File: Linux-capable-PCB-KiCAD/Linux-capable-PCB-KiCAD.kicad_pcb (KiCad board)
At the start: 4 copper layers, 168 parts, among them J1 UART_CONN, J2 GPIO_CONN, J3 USB_A, J4 USB_A, J5 Micro_SD_Card_Det, J6 MIC_DIFF_IN, J7 Barrel_Jack, U1 A33, U10 TPS62130, U11 AP131-25, U12 TPS62130, U13 TPS62130, U2 MMA8425Q_Gsensor, U3 SRV05-4, U4 MIPI_DSI_Raspberry, U5 SRV05-4, U6 SRV05-4, U7 ESP8089, U8 HTQ4G63AFR-PCB, U9 TPS62130, Y1 24MHz, Y2 32.768kHz, Y3 26 MHz

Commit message: SD card move
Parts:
- moved J5 47.5 mm to (143.5, 98.3), turned to 180 degrees
- moved U4 12.0 mm to (164.4, 100.2)
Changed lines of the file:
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@@
   )
   (footprint "Connector_Card:microSD_HC_Molex_104031-0811" (layer "F.Cu")
-    (at 143.51 50.8)
+    (at 143.5 98.33 180)
     (descr "1.10mm Pitch microSD Memory Card Connector, Surface Mount, Push-Pull Type, 1.42mm Height, with Detect Switch (https://www.molex.com/pdm_docs/sd/1040310811_sd.pdf)")
     (tags "microSD SD molex")
@@
     (fp_arc (start 5.095 -9.7) (mid 5.448553 -9.553553) (end 5.595 -9.2) (layer "F.Fab") (width 0.1))
     (fp_arc (start -3.26 -4.3) (mid -3.613553 -4.446447) (end -3.76 -4.8) (layer "F.Fab") (width 0.1))
-    (pad "1" smd rect locked (at -3.105 -5.45) (size 0.85 1.1) (layers "F.Cu" "F.Paste" "F.Mask")
+    (pad "1" smd rect locked (at -3.105 -5.45 180) (size 0.85 1.1) (layers "F.Cu" "F.Paste" "F.Mask")
       (net 53 "/A33_GPIO/SD_DAT2"))
-    (pad "2" smd rect locked (at -2.005 -5.45) (size 0.85 1.1) (layers "F.Cu" "F.Paste" "F.Mask")
+    (pad "2" smd rect locked (at -2.005 -5.45 180) (size 0.85 1.1) (layers "F.Cu" "F.Paste" "F.Mask")
       (net 55 "/A33_GPIO/SD_DAT3"))
-    (pad "3" smd rect locked (at -0.905 -5.45) (size 0.85 1.1) (layers "F.Cu" "F.Paste" "F.Mask")
+    (pad "3" smd rect locked (at -0.905 -5.45 180) (size 0.85 1.1) (layers "F.Cu" "F.Paste" "F.Mask")
       (net 56 "/A33_GPIO/SD_CMD"))
-    (pad "4" smd rect locked (at 0.195 -5.45) (size 0.85 1.1) (layers "F.Cu" "F.Paste" "F.Mask")
+    (pad "4" smd rect locked (at 0.195 -5.45 180) (size 0.85 1.1) (layers "F.Cu" "F.Paste" "F.Mask")
       (net 14 "Net-(C33-Pad1)"))
-    (pad "5" smd rect locked (at 1.295 -5.45) (size 0.85 1.1) (layers "F.Cu" "F.Paste" "F.Mask")
+    (pad "5" smd rect locked (at 1.295 -5.45 180) (size 0.85 1.1) (layers "F.Cu" "F.Paste" "F.Mask")
       (net 57 "/A33_GPIO/SD_CLK"))
-    (pad "6" smd rect locked (at 2.395 -5.45) (size 0.85 1.1) (layers "F.Cu" "F.Paste" "F.Mask")
-      (net 3 "GND"))
-    (pad "7" smd rect locked (at 3.495 -5.45) (size 0.85 1.1) (layers "F.Cu" "F.Paste" "F.Mask")
+    (pad "6" smd rect locked (at 2.395 -5.45 180) (size 0.85 1.1) (layers "F.Cu" "F.Paste" "F.Mask")
+      (net 3 "GND"))
+    (pad "7" smd rect locked (at 3.495 -5.45 180) (size 0.85 1.1) (layers "F.Cu" "F.Paste" "F.Mask")
       (net 58 "/A33_GPIO/SD_DAT0"))
-    (pad "8" smd rect locked (at 4.545 -5.45) (size 0.75 1.1) (layers "F.Cu" "F.Paste" "F.Mask")
+    (pad "8" smd rect locked (at 4.545 -5.45 180) (size 0.75 1.1) (layers "F.Cu" "F.Paste" "F.Mask")
       (net 54 "/A33_GPIO/SD_DAT1"))
-    (pad "9" smd rect locked (at -5.74 0.7) (size 1.2 1) (layers "F.Cu" "F.Paste" "F.Mask")
-      (net 3 "GND"))
-    (pad "10" smd rect locked (at -5.74 4.4) (size 1.2 1) (layers "F.Cu" "F.Paste" "F.Mask")
+    (pad "9" smd rect locked (at -5.74 0.7 180) (size 1.2 1) (layers "F.Cu" "F.Paste" "F.Mask")
+      (net 3 "GND"))
+    (pad "10" smd rect locked (at -5.74 4.4 180) (size 1.2 1) (layers "F.Cu" "F.Paste" "F.Mask")
       (net 59 "/A33_GPIO/SD_DET"))
-    (pad "11" smd rect locked (at -2.24 5.375) (size 1.9 1.35) (layers "F.Cu" "F.Paste" "F.Mask")
-      (net 3 "GND"))
-    (pad "11" smd rect locked (at -5.565 -5.325) (size 1.55 1.35) (layers "F.Cu" "F.Paste" "F.Mask")
-      (net 3 "GND"))
-    (pad "11" smd rect locked (at 5.755 -5.1) (size 1.17 1.8) (layers "F.Cu" "F.Paste" "F.Mask")
-      (net 3 "GND"))
-    (pad "11" smd rect locked (at 3.73 5.375) (size 1.9 1.35) (layers "F.Cu" "F.Paste" "F.Mask")
+    (pad "11" smd rect locked (at -2.24 5.375 180) (size 1.9 1.35) (layers "F.Cu" "F.Paste" "F.Mask")
+      (net 3 "GND"))
+    (pad "11" smd rect locked (at -5.565 -5.325 180) (size 1.55 1.35) (layers "F.Cu" "F.Paste" "F.Mask")
+      (net 3 "GND"))
+    (pad "11" smd rect locked (at 5.755 -5.1 180) (size 1.17 1.8) (layers "F.Cu" "F.Paste" "F.Mask")
+      (net 3 "GND"))
+    (pad "11" smd rect locked (at 3.73 5.375 180) (size 1.9 1.35) (layers "F.Cu" "F.Paste" "F.Mask")
       (net 3 "GND"))
     (model "${KISYS3DMOD}/Connector_Card.3dshapes/microSD_HC_Molex_104031-0811.wrl"
@@
   )
   (footprint "Connector_FFC-FPC:Molex_502244-1530_1x15-1MP_P0.5mm_Horizontal" (layer "F.Cu")
-    (at 152.4 100.33)
+    (at 164.4 100.17)
     (descr "Molex 0.50mm Pitch Easy-On Type FFC/FPC Connector, For LVDS, 2.33mm Height, Right Angle, Surface Mount, ZIF, Bottom Contact Style, 15 Circuits (http://www.molex.com/pdm_docs/sd/5022441530_sd.pdf)")
     (tags "molex FFC/FPC connector Pitch 0.5mm right angle")

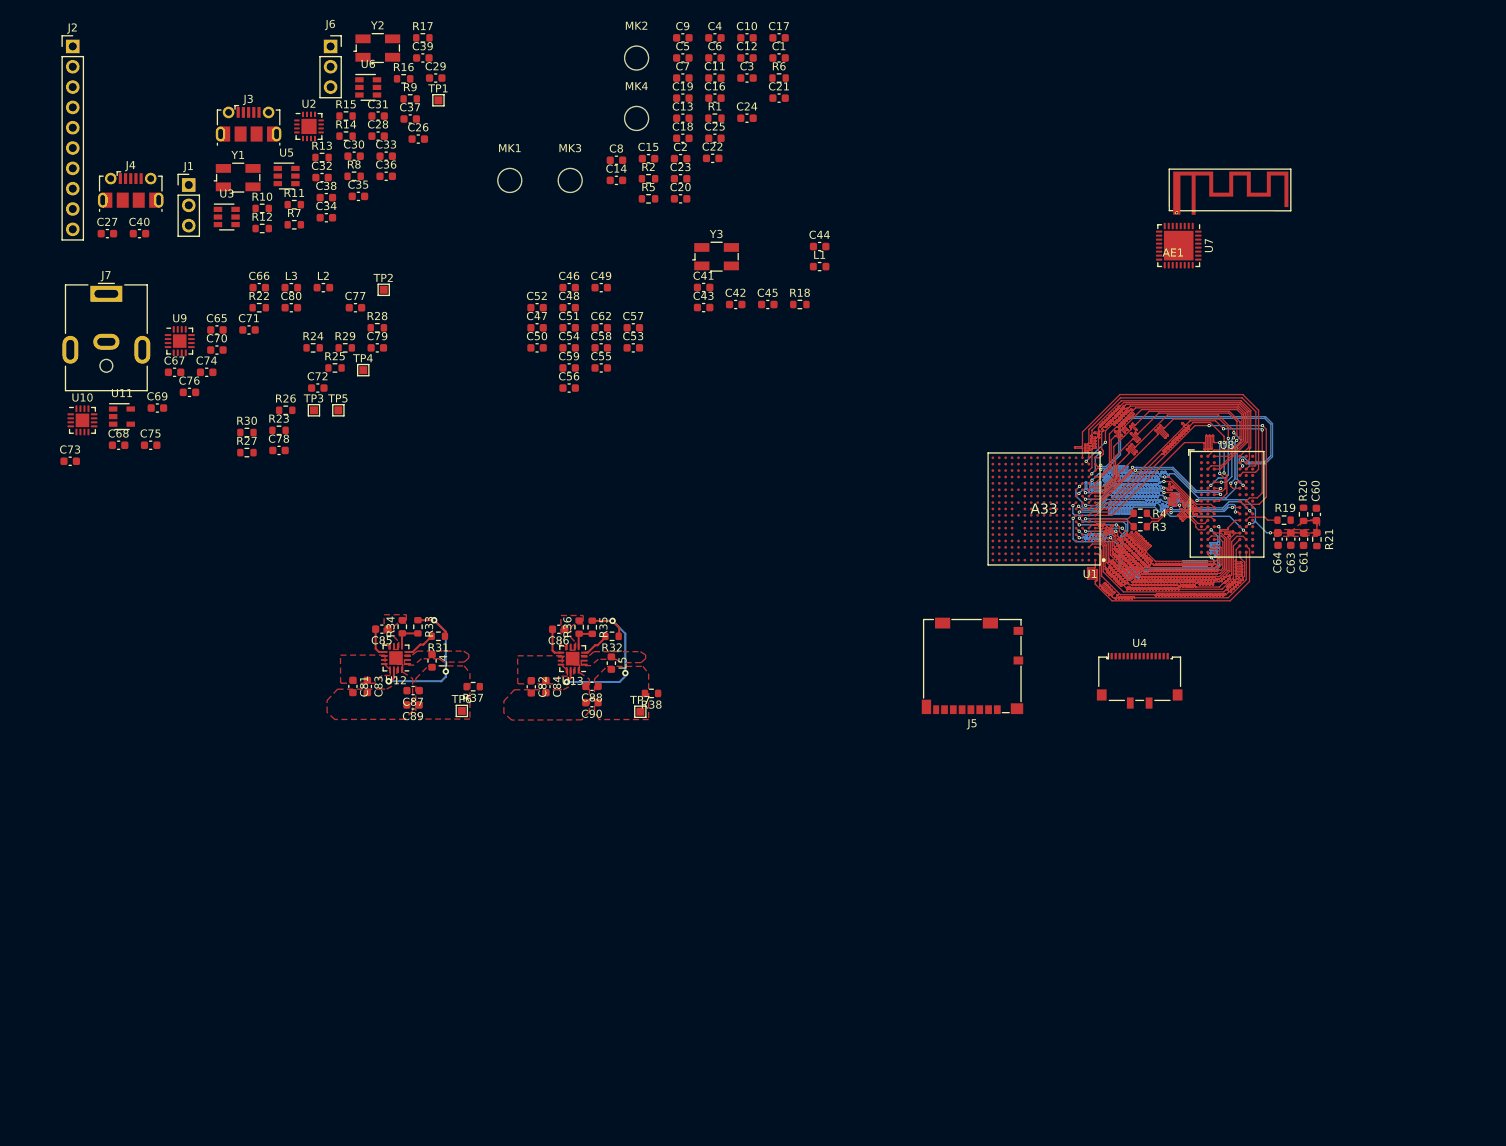
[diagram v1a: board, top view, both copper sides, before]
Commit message: Dodao 3.3V na SD karticu, treba zamjeniti SD konektor, zavrsio napjanje, treba izracunati vrijednosti otpornika i footprint preci za komponente
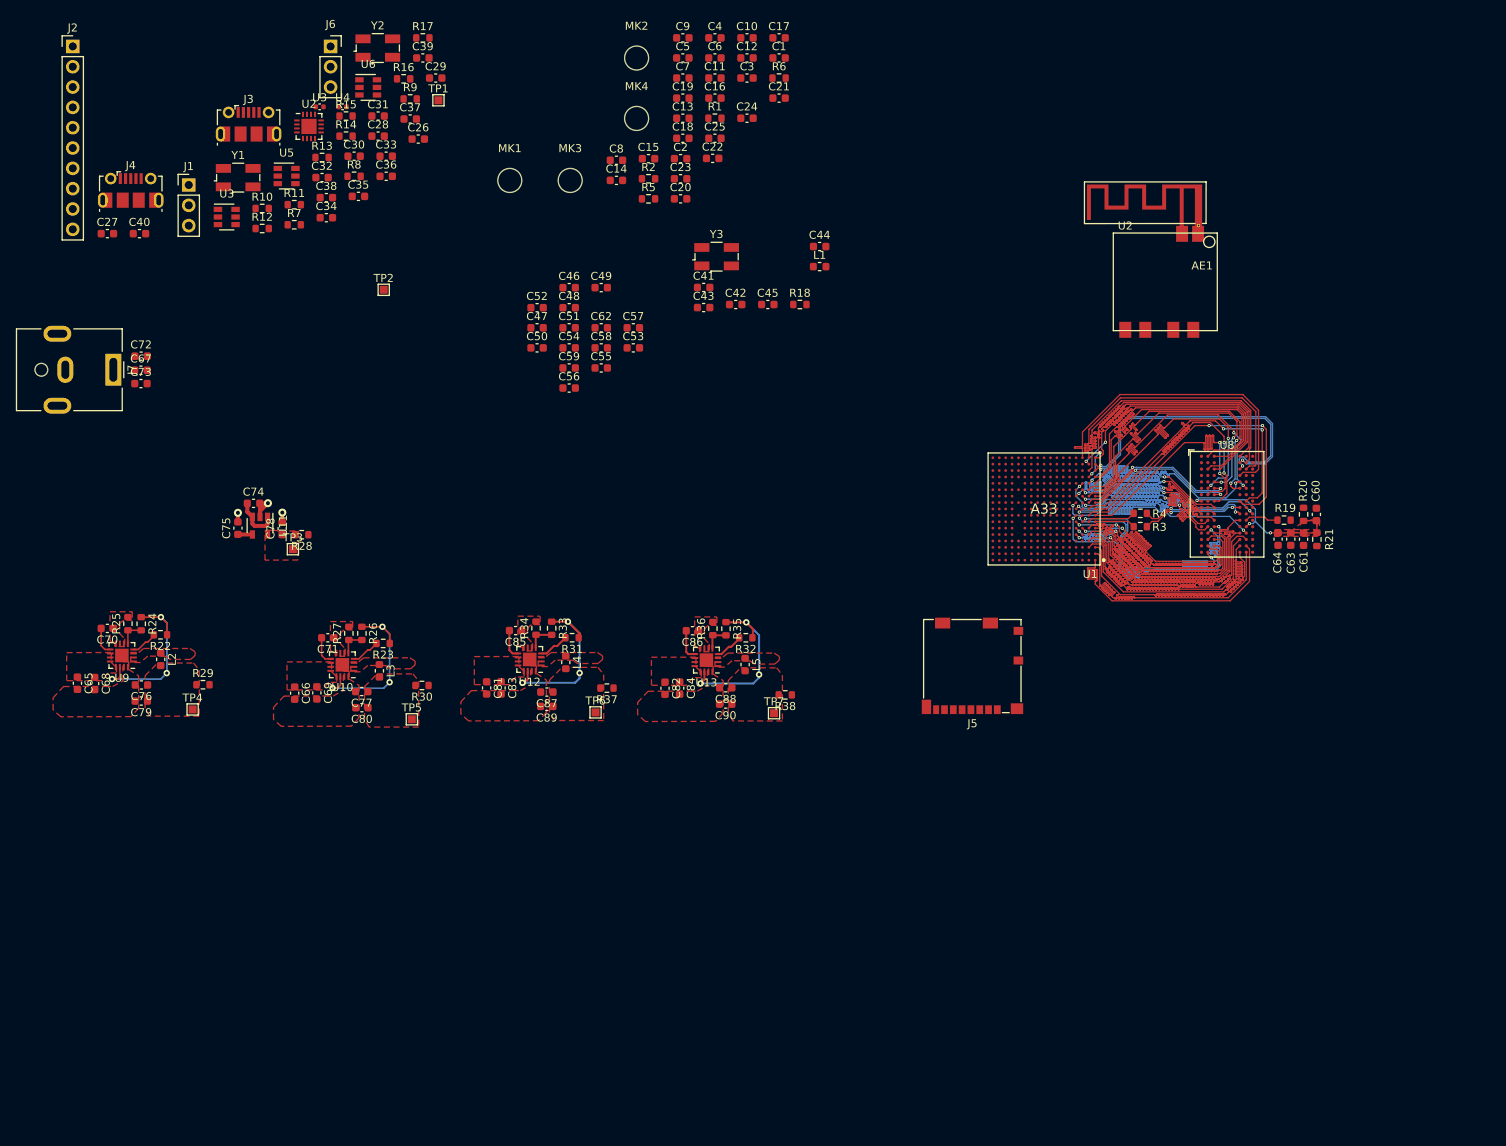
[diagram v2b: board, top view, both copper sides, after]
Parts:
- removed U7: ESP8089, Package_DFN_QFN:QFN-32-1EP_5x5mm_P0.5mm_EP3.7x3.7mm
- added U2: RTL8188CUS, realtek:RTL8188CUS, F.Cu at (167.6, 50.3)
- added U3: 100nF, Capacitor_SMD:C_0402_1005Metric, F.Cu at (61.9, 28.4)
- U4: value MIPI_DSI_Raspberry -> 22uF; footprint Connector_FFC-FPC:Molex_502244-1530_1x15-1MP_P0.5mm_Horizontal -> Capacitor_SMD:C_0402_1005Metric
- moved U4 122.8 mm to (64.8, 28.4)
- moved C79 53.1 mm to (39.6, 102.7), turned to 180 degrees
- moved C66 50.9 mm to (58.8, 101.7), turned to -90 degrees
- moved C80 50.8 mm to (67.2, 103.5), turned to 180 degrees
- moved L2 50.7 mm to (42.0, 97.5), turned to -90 degrees
- moved L3 49.1 mm to (69.4, 98.9), turned to -90 degrees
- moved C77 48.0 mm to (67.2, 101.5), turned to 180 degrees
- moved TP4 47.5 mm to (46.0, 103.8)
- moved C65 47.5 mm to (31.6, 100.5), turned to -90 degrees
- moved R29 45.7 mm to (47.3, 100.7)
- moved U10 44.6 mm to (64.7, 98.2), turned to 180 degrees
- moved R22 42.7 mm to (42.0, 94.4), turned to 180 degrees
- moved R25 41.1 mm to (37.9, 93.0), turned to 90 degrees
- moved C69 40.8 mm to (61.5, 101.7), turned to -90 degrees
- moved R24 40.6 mm to (39.6, 93.0), turned to -90 degrees
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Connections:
- AE1 pad 1: /A33_GPIO/WiFi_chip/WIFI_ANT -> Net-(AE1-Pad1)
- C29 pad 1: Net-(C29-Pad1) -> unconnected-(C29-Pad1)
- J4 pad 1: Net-(J3-Pad1) -> Net-(J4-Pad1)
- U1 pad A10: Net-(U1-PadA10) -> unconnected-(U1-PadA10)
- U1 pad A11: Net-(U1-PadA11) -> unconnected-(U1-PadA11)
- U1 pad A12: Net-(U1-PadA12) -> unconnected-(U1-PadA12)
- U1 pad A13: /A33_GPIO/SD_D3 -> unconnected-(U1-PadA13)
- U1 pad A14: /A33_GPIO/SD_CLK -> unconnected-(U1-PadA14)
- U1 pad A15: /A33_GPIO/SD_D1 -> unconnected-(U1-PadA15)
- U1 pad A16: Net-(U1-PadA16) -> unconnected-(U1-PadA16)
- U1 pad A17: /A33_GPIO/WIFI_EN -> unconnected-(U1-PadA17)
- U1 pad A2: Net-(U1-PadA2) -> unconnected-(U1-PadA2)
- U1 pad A7: Net-(U1-PadA7) -> unconnected-(U1-PadA7)
- U1 pad A8: Net-(U1-PadA8) -> unconnected-(U1-PadA8)
- U1 pad A9: Net-(U1-PadA9) -> unconnected-(U1-PadA9)
- U1 pad B10: Net-(U1-PadB10) -> unconnected-(U1-PadB10)
- U1 pad B11: Net-(U1-PadB11) -> unconnected-(U1-PadB11)
- U1 pad B13: /A33_GPIO/SD_D2 -> unconnected-(U1-PadB13)
- U1 pad B14: /A33_GPIO/SD_CMD -> unconnected-(U1-PadB14)
- U1 pad B15: /A33_GPIO/SD_D0 -> unconnected-(U1-PadB15)
- U1 pad B16: Net-(U1-PadB16) -> unconnected-(U1-PadB16)
- U1 pad B17: Net-(U1-PadB17) -> unconnected-(U1-PadB17)
- U1 pad B2: Net-(U1-PadB2) -> unconnected-(U1-PadB2)
- U1 pad B7: Net-(U1-PadB7) -> unconnected-(U1-PadB7)
- U1 pad B8: Net-(U1-PadB8) -> unconnected-(U1-PadB8)
- U1 pad B9: Net-(U1-PadB9) -> unconnected-(U1-PadB9)
- U1 pad C10: Net-(U1-PadC10) -> unconnected-(U1-PadC10)
- U1 pad C11: Net-(U1-PadC11) -> unconnected-(U1-PadC11)
- U1 pad C12: Net-(U1-PadC12) -> unconnected-(U1-PadC12)
- U1 pad C13: Net-(U1-PadC13) -> unconnected-(U1-PadC13)
- U1 pad C14: Net-(U1-PadC14) -> unconnected-(U1-PadC14)
- U1 pad C15: Net-(U1-PadC15) -> unconnected-(U1-PadC15)
- U1 pad C16: Net-(U1-PadC16) -> unconnected-(U1-PadC16)
- U1 pad C17: Net-(U1-PadC17) -> unconnected-(U1-PadC17)
- U1 pad C3: Net-(U1-PadC3) -> unconnected-(U1-PadC3)
- U1 pad C4: Net-(U1-PadC4) -> unconnected-(U1-PadC4)
- U1 pad D10: Net-(U1-PadD10) -> unconnected-(U1-PadD10)
- U1 pad D11: Net-(U1-PadD11) -> unconnected-(U1-PadD11)
- U1 pad D12: Net-(U1-PadD12) -> unconnected-(U1-PadD12)
- U1 pad D13: Net-(U1-PadD13) -> unconnected-(U1-PadD13)
- U1 pad D14: /A33_GPIO/G_INT2 -> unconnected-(U1-PadD14)
- U1 pad D15: /A33_GPIO/G_INT1 -> unconnected-(U1-PadD15)
- U1 pad D16: /A33_GPIO/G_SDA -> unconnected-(U1-PadD16)
- U1 pad D17: /A33_GPIO/G_SCL -> unconnected-(U1-PadD17)
- U1 pad D3: Net-(U1-PadD3) -> unconnected-(U1-PadD3)
- U1 pad D4: Net-(U1-PadD4) -> unconnected-(U1-PadD4)
- U1 pad E14: Net-(U1-PadE14) -> unconnected-(U1-PadE14)
- U1 pad E15: Net-(U1-PadE15) -> unconnected-(U1-PadE15)
- U1 pad E16: Net-(U1-PadE16) -> unconnected-(U1-PadE16)
- U1 pad E17: Net-(U1-PadE17) -> unconnected-(U1-PadE17)
- U1 pad F14: Net-(U1-PadF14) -> unconnected-(U1-PadF14)
- U1 pad F15: Net-(U1-PadF15) -> unconnected-(U1-PadF15)
- U1 pad F16: Net-(U1-PadF16) -> unconnected-(U1-PadF16)
- U1 pad F17: Net-(U1-PadF17) -> unconnected-(U1-PadF17)
- U1 pad G15: Net-(U1-PadG15) -> unconnected-(U1-PadG15)
- U1 pad H14: Net-(U1-PadH14) -> unconnected-(U1-PadH14)
- U1 pad H15: Net-(U1-PadH15) -> unconnected-(U1-PadH15)
- U1 pad H16: Net-(U1-PadH16) -> unconnected-(U1-PadH16)
- U1 pad J14: Net-(U1-PadJ14) -> unconnected-(U1-PadJ14)
- U1 pad J15: Net-(U1-PadJ15) -> unconnected-(U1-PadJ15)
- U1 pad J16: Net-(U1-PadJ16) -> unconnected-(U1-PadJ16)
- U1 pad J17: Net-(U1-PadJ17) -> unconnected-(U1-PadJ17)
- U1 pad K14: Net-(U1-PadK14) -> unconnected-(U1-PadK14)
- U1 pad K15: Net-(U1-PadK15) -> unconnected-(U1-PadK15)
- U1 pad L14: Net-(U1-PadL14) -> unconnected-(U1-PadL14)
- U1 pad L15: Net-(U1-PadL15) -> unconnected-(U1-PadL15)
- U1 pad L7: Net-(U1-PadL7) -> unconnected-(U1-PadL7)
- U1 pad M15: Net-(U1-PadM15) -> unconnected-(U1-PadM15)
- U1 pad N15: Net-(U1-PadN15) -> unconnected-(U1-PadN15)
- U1 pad N16: Net-(U1-PadN16) -> unconnected-(U1-PadN16)
- U1 pad N17: Net-(U1-PadN17) -> unconnected-(U1-PadN17)
- U1 pad N5: Net-(U1-PadN5) -> unconnected-(U1-PadN5)
- U1 pad N7: Net-(U1-PadN7) -> unconnected-(U1-PadN7)
- U1 pad P10: Net-(U1-PadP10) -> unconnected-(U1-PadP10)
- U1 pad P11: Net-(U1-PadP11) -> unconnected-(U1-PadP11)
- U1 pad P12: Net-(U1-PadP12) -> unconnected-(U1-PadP12)
- U1 pad P13: Net-(U1-PadP13) -> unconnected-(U1-PadP13)
- U1 pad P14: Net-(U1-PadP14) -> unconnected-(U1-PadP14)
- U1 pad P15: Net-(U1-PadP15) -> unconnected-(U1-PadP15)
- U1 pad P16: Net-(U1-PadP16) -> unconnected-(U1-PadP16)
- U1 pad P4: /A33_GPIO/DSI1_DP0 -> unconnected-(U1-PadP4)
- U1 pad P5: /A33_GPIO/DSI1_DP1 -> unconnected-(U1-PadP5)
- U1 pad P6: Net-(U1-PadP6) -> unconnected-(U1-PadP6)
- U1 pad P7: Net-(U1-PadP7) -> unconnected-(U1-PadP7)
- U1 pad P8: Net-(U1-PadP8) -> unconnected-(U1-PadP8)
- U1 pad P9: Net-(U1-PadP9) -> unconnected-(U1-PadP9)
- U1 pad R10: Net-(U1-PadR10) -> unconnected-(U1-PadR10)
- U1 pad R11: Net-(U1-PadR11) -> unconnected-(U1-PadR11)
- U1 pad R12: Net-(U1-PadR12) -> unconnected-(U1-PadR12)
- U1 pad R13: Net-(U1-PadR13) -> unconnected-(U1-PadR13)
- U1 pad R14: Net-(U1-PadR14) -> unconnected-(U1-PadR14)
- U1 pad R15: Net-(U1-PadR15) -> unconnected-(U1-PadR15)
- U1 pad R4: /A33_GPIO/DSI1_DN0 -> unconnected-(U1-PadR4)
- U1 pad R5: /A33_GPIO/DSI1_DN1 -> unconnected-(U1-PadR5)
- U1 pad R6: Net-(U1-PadR6) -> unconnected-(U1-PadR6)
- U1 pad R7: Net-(U1-PadR7) -> unconnected-(U1-PadR7)
- U1 pad R8: Net-(U1-PadR8) -> unconnected-(U1-PadR8)
- U1 pad R9: Net-(U1-PadR9) -> unconnected-(U1-PadR9)
- U1 pad T10: Net-(U1-PadT10) -> unconnected-(U1-PadT10)
- U1 pad T11: Net-(U1-PadT11) -> unconnected-(U1-PadT11)
- U1 pad T12: Net-(U1-PadT12) -> unconnected-(U1-PadT12)
- U1 pad T13: Net-(U1-PadT13) -> unconnected-(U1-PadT13)
- U1 pad T14: Net-(U1-PadT14) -> unconnected-(U1-PadT14)
- U1 pad T15: Net-(U1-PadT15) -> unconnected-(U1-PadT15)
- U1 pad T5: /A33_GPIO/DSI1_CP -> unconnected-(U1-PadT5)
- U1 pad T6: Net-(U1-PadT6) -> unconnected-(U1-PadT6)
- U1 pad T7: Net-(U1-PadT7) -> unconnected-(U1-PadT7)
- U1 pad T8: Net-(U1-PadT8) -> unconnected-(U1-PadT8)
- U1 pad T9: Net-(U1-PadT9) -> unconnected-(U1-PadT9)
- U1 pad U10: Net-(U1-PadU10) -> unconnected-(U1-PadU10)
- U1 pad U11: Net-(U1-PadU11) -> unconnected-(U1-PadU11)
- U1 pad U12: Net-(U1-PadU12) -> unconnected-(U1-PadU12)
- U1 pad U14: Net-(U1-PadU14) -> unconnected-(U1-PadU14)
- U1 pad U15: Net-(U1-PadU15) -> unconnected-(U1-PadU15)
- U1 pad U5: /A33_GPIO/DSI1_CN -> unconnected-(U1-PadU5)
- U1 pad U6: Net-(U1-PadU6) -> unconnected-(U1-PadU6)
- U1 pad U7: Net-(U1-PadU7) -> unconnected-(U1-PadU7)
- U1 pad U8: Net-(U1-PadU8) -> unconnected-(U1-PadU8)
- U1 pad U9: Net-(U1-PadU9) -> unconnected-(U1-PadU9)
- U4 pad 1: GND -> +3V3
- U4 pad 2: /A33_GPIO/DSI1_DN1 -> GND
- U8 pad J1: Net-(U8-PadJ1) -> unconnected-(U8-PadJ1)
- U8 pad J9: Net-(U8-PadJ9) -> unconnected-(U8-PadJ9)
- U8 pad L1: Net-(U8-PadL1) -> unconnected-(U8-PadL1)
- U8 pad L9: Net-(U8-PadL9) -> unconnected-(U8-PadL9)
- U8 pad M7: Net-(U8-PadM7) -> unconnected-(U8-PadM7)
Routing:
- net Net-(C77-Pad1): track 0.00 -> 22.0 mm, vias 0 -> 3
- net Net-(C76-Pad1): track 0.00 -> 21.8 mm, vias 0 -> 3
- net GND: track 0.00 -> 7.75 mm, vias 0 -> 3
- net +3V3: track 0.00 -> 5.80 mm
- net Net-(R23-Pad2): track 0.00 -> 3.61 mm
- net Net-(C71-Pad2): track 0.00 -> 3.52 mm
- net Net-(C70-Pad2): track 0.00 -> 3.49 mm
- net Net-(R22-Pad2): track 0.00 -> 3.38 mm
- net Net-(R24-Pad2): track 0.00 -> 3.35 mm
- net Net-(R26-Pad2): track 0.00 -> 3.30 mm
- net Net-(C75-Pad1): track 0.00 -> 1.82 mm
- net Net-(AE1-Pad1): track 0.00 -> 1.03 mm
- added copper zone on F.Cu, net Net-(C76-Pad1)
- added copper zone on F.Cu, net Net-(C77-Pad1)
- added copper zone on F.Cu, net Net-(C78-Pad1)
- added copper zone on F.Cu, net Net-(L2-Pad1)
- added copper zone on F.Cu, net Net-(L3-Pad1)

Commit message: message
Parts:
- removed C12: 22u, Capacitor_SMD:C_0603_1608Metric
- removed C16, C19, C4, C42, C43, C44, C45, C50, C53, C8: 100n, Capacitor_SMD:C_0603_1608Metric
- removed C41: 5.6p, Capacitor_SMD:C_0603_1608Metric
- removed J3: USB_A, Connector_USB:USB_Micro-B_Molex-105017-0001
- removed J5: Micro_SD_Card_Det, Connector_Card:microSD_HC_Molex_104031-0811
- removed L1: NC, Inductor_SMD:L_0603_1608Metric
- removed the U2 at (60.6, 30.9)
- removed U3, U6: SRV05-4, Package_TO_SOT_SMD:SOT-23-6
- removed U4: 22uF, Capacitor_SMD:C_0402_1005Metric
- added Q1: Q_PMOS_GSD, Package_TO_SOT_SMD:SC-59_Handsoldering, F.Cu at (110.7, 69.7)
- added Q2: BC547, Package_TO_SOT_SMD:SC-59_Handsoldering, F.Cu at (109.5, 63.0)
- added TP8: Test_Point, TestPoint:TestPoint_Pad_1.0x1.0mm, F.Cu at (142.9, 93.6)
- AE1, C10, C11, C13, C14, C15, C17, C18, C20, C21, C22, C23, C24, C25, C3, C33, C34, C35, C46, C47, C48, C49, C5, C51, C54, C57, C58, C59, C6, C62, C7, C9, R11, R12, R13, R14, R16, R6, R9, TP1, U2: moved to B.Cu
- C26: renamed from U3; footprint Capacitor_SMD:C_0402_1005Metric -> Resistor_SMD:R_0603_1608Metric
- C27: value C -> 22uF; footprint Capacitor_SMD:C_0603_1608Metric -> Resistor_SMD:R_0603_1608Metric
- R18: value R -> 100k; moved to B.Cu
- U5: value SRV05-4 -> SD_card_slot; footprint Package_TO_SOT_SMD:SOT-23-6 -> SD_Card_9_pin:SD_Card_9_pin_slot
- moved MK4 134.8 mm to (206.3, 114.7)
- moved C27 118.1 mm to (151.3, 66.6), turned to 90 degrees
- moved C75 116.9 mm to (166.2, 57.5), turned to -45 degrees
- moved C74 114.6 mm to (167.0, 61.1), turned to -135 degrees
- moved U11 112.0 mm to (164.5, 59.7), turned to 135 degrees
- moved R12 109.9 mm to (153.0, 92.9), turned to -90 degrees
- moved C40 109.3 mm to (143.6, 77.0)
- moved R11 107.1 mm to (154.1, 89.4), turned to -90 degrees
- moved C78 106.9 mm to (162.2, 61.4), turned to -45 degrees
- moved R13 105.0 mm to (151.8, 89.4), turned to -90 degrees
- moved TP3 103.6 mm to (159.5, 60.5), turned to -135 degrees
- moved R14 102.3 mm to (147.4, 92.9), turned to -90 degrees
- moved U5 102.3 mm to (145.3, 90.0)
- moved R28 102.1 mm to (160.0, 62.6), turned to 45 degrees
- moved C34 100.3 mm to (150.0, 91.8), turned to 180 degrees
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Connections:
- C27 pad 1: Net-(C27-Pad1) -> +3V3
- C33 pad 1: Net-(C33-Pad1) -> +3V3
- C34 pad 1: Net-(C33-Pad1) -> +3V3
- R11 pad 2: Net-(C33-Pad1) -> +3V3
- R12 pad 2: Net-(C33-Pad1) -> +3V3
- R13 pad 2: Net-(C33-Pad1) -> +3V3
- R14 pad 2: Net-(C33-Pad1) -> +3V3
- R15 pad 2: Net-(C33-Pad1) -> +3V3
- R16 pad 1: /A33_GPIO/SD_DET -> Net-(R16-Pad1)
- R16 pad 2: Net-(C33-Pad1) -> +3V3
- R18 pad 2: Net-(R18-Pad2) -> Net-(R16-Pad1)
- R38 pad 1: +1V5 -> +1V35
- U1 pad C5: /A33_GPIO/SCL0 -> unconnected-(U1-PadC5)
- U1 pad D5: /A33_GPIO/SDA0 -> unconnected-(U1-PadD5)
- U1 pad G14: /A33_GPIO/SD_DET -> Net-(R16-Pad1)
- U5 pad 1: /A33_GPIO/GPIO3 -> /A33_GPIO/SD_DAT2
- U5 pad 2: GND -> /A33_GPIO/SD_DAT3
- U5 pad 3: /A33_GPIO/GPIO4 -> /A33_GPIO/SD_CMD
- U5 pad 4: /A33_GPIO/GPIO5 -> +3V3
- U5 pad 5: +3V3 -> /A33_GPIO/SD_CLK
- U5 pad 6: /A33_GPIO/GPIO6 -> GND
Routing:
- net +1V5: track 0.00 -> 40.4 mm, vias 0 -> 16
- net /A33_GPIO/USB0-DN: track 0.00 -> 26.0 mm
- net /A33_GPIO/USB0-DP: track 0.00 -> 25.4 mm
- net +1V1: track 0.00 -> 22.3 mm, vias 0 -> 10
- net /RAM/DMU: track 0.00 -> 18.7 mm, vias 0 -> 2
- net /DVREF: track 0.00 -> 13.2 mm, vias 0 -> 2
- net +2V5: track 0.00 -> 12.7 mm, vias 0 -> 2
- net /A33_GPIO/SD_DAT0: track 0.00 -> 12.0 mm, vias 0 -> 1
- net /A33_GPIO/SD_DAT1: track 0.00 -> 10.8 mm, vias 0 -> 2
- net /A33_GPIO/SD_DAT3: track 0.00 -> 10.5 mm, vias 0 -> 1
- net /A33_GPIO/SD_CLK: track 0.00 -> 8.82 mm, vias 0 -> 2
- net +1V35: track 0.00 -> 8.52 mm, vias 0 -> 36
- net +3V3: track 5.80 -> 14.0 mm, vias 0 -> 3
- net /A33_GPIO/SD_CMD: track 0.00 -> 8.02 mm, vias 0 -> 1
- net /A33_GPIO/SD_DAT2: track 0.00 -> 7.88 mm, vias 0 -> 1
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- added copper zone on F.Cu, net +1V1
- added copper zone on In1.Cu, net +1V1
- added copper zone on F.Cu, net +1V35
- added copper zone on In1.Cu, net +1V35
- added copper zone on F.Cu, net +3V3
- added copper zone on In1.Cu, net +3V3
- added copper zone on F.Cu, net /DVREF
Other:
- board outline added: 90.1 x 59.2 mm
